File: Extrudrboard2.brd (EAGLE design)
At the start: 43.2 x 46.7 mm, 7 parts, among them U1 SN74HC138N

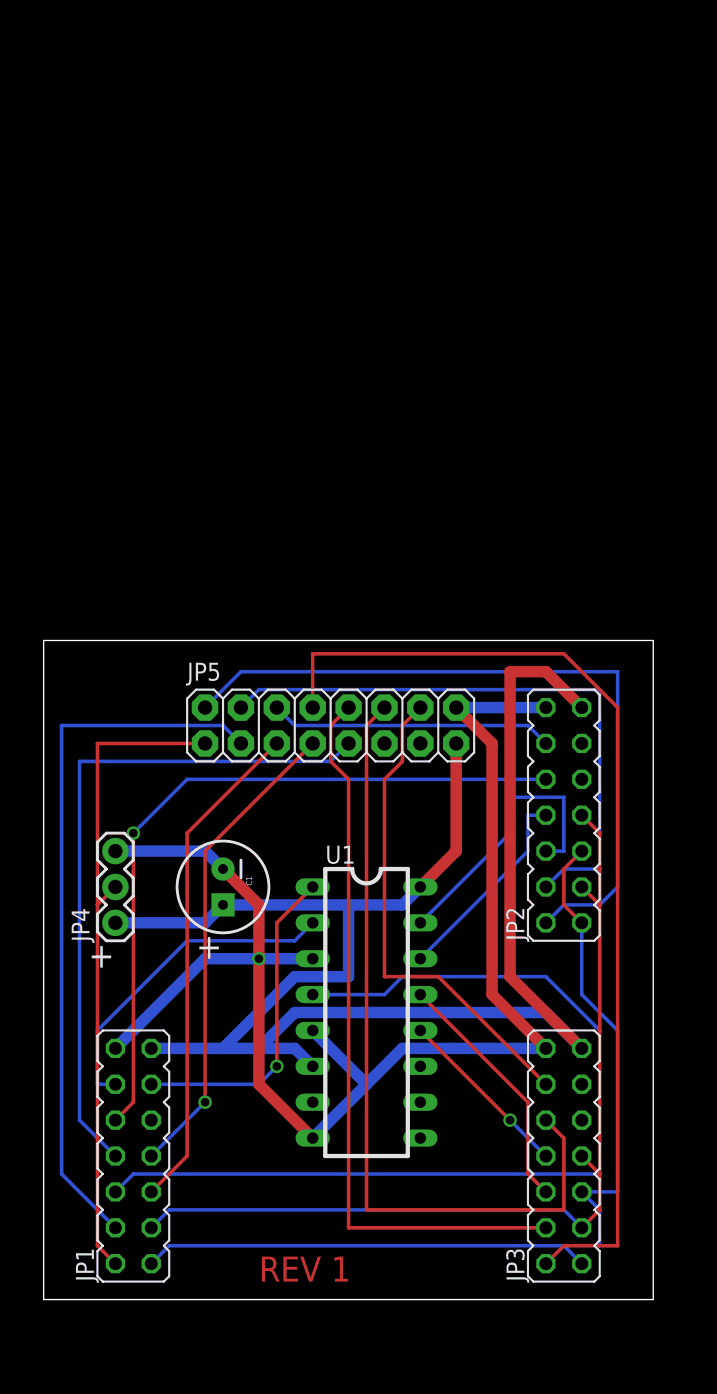
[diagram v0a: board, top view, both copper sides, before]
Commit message: Multiplex STEP instead of ENABLE.
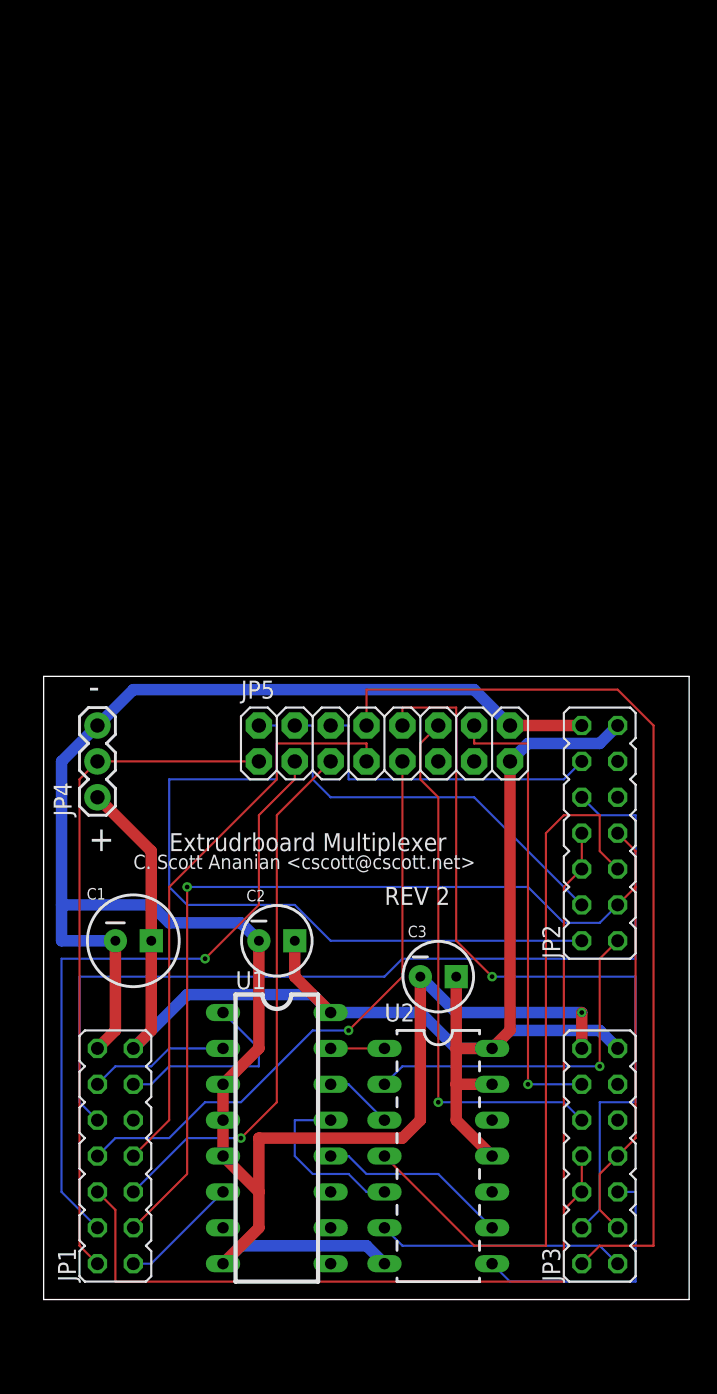
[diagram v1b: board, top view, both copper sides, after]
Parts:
- added C2, C3: 100nF, SparkFun:CPOL-RADIAL-10UF-25V
- added U2: SN74HC04, SparkFun:DIL14
- C1: value (none) -> 22uF
- moved U1 10.9 mm to (16.5, 14.0)
- moved JP4 8.98 mm to (3.81, 38.1)
- moved C1 7.41 mm to (6.35, 27.9), turned to 0 degrees
- moved JP5 4.02 mm to (15.2, 40.6)
- moved JP2 2.84 mm to (39.4, 35.6)
- moved JP3 2.54 mm to (39.4, 12.7)
- moved JP1 1.27 mm to (5.08, 12.7)
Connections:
- removed net A-ENABLE: JP2.6, U1.15
- removed net B-ENABLE: JP2.8, U1.14
- removed net C-ENABLE: JP3.6, U1.13
- removed net D-ENABLE: JP3.8, U1.12
- new net !A-STEP: U1.15, U2.1
- new net !B-STEP: U1.14, U2.3
- new net !C-STEP: U1.13, U2.5
- new net !D-STEP: U1.12, U2.9
- new net A-STEP: JP2.1, U2.2
- new net B-STEP: JP2.5, U2.4
- new net C-STEP: JP3.1, U2.6
- new net D-STEP: JP3.5, U2.8
- net E-ENABLE: now also JP2.6, JP2.8, JP3.6, JP3.8; no longer U1.4
- net E-STEP: now also U1.6; no longer JP2.1, JP2.5, JP3.1, JP3.5
- net GND: now also C2.2, C3.2, U1.4, U2.7
- net VCC: now also C2.1, C3.1, U2.11, U2.13, U2.14; no longer U1.6
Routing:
- net E-STEP: track 67.2 -> 8.45 mm
- net GND: track 104.1 -> 159.1 mm
- net B-STEP: track 0.00 -> 51.9 mm
- net A-STEP: track 0.00 -> 25.2 mm, vias 0 -> 1
- net E-DIR: track 65.4 -> 89.6 mm, vias 0 -> 1
- net A-ENABLE: track 20.4 -> 0.00 mm
- net X2_HOTENDA: track 56.9 -> 38.4 mm, vias 0 -> 1
- net D-STEP: track 0.00 -> 18.3 mm
- net C-ENABLE: track 17.7 -> 0.00 mm
- net C-STEP: track 0.00 -> 17.6 mm
- net X1_BTHERM: track 43.0 -> 27.8 mm
- net B-ENABLE: track 14.6 -> 0.00 mm
- net E_MUX1: track 23.5 -> 9.94 mm
- net !D-STEP: track 0.00 -> 13.5 mm
- net FAN2: track 51.6 -> 65.1 mm, vias 1 -> 0
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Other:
- board size 43.2 x 46.7 mm -> 45.7 x 44.1 mm
- board text added: "-"
- board text added: "CSA 2017-07-19"
- board text added: "REV 2"
- board text removed: "2017-07-18"
- board text removed: "REV 1"

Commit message: Rename Extrudrboard to Extrudrboard2 for clarity.
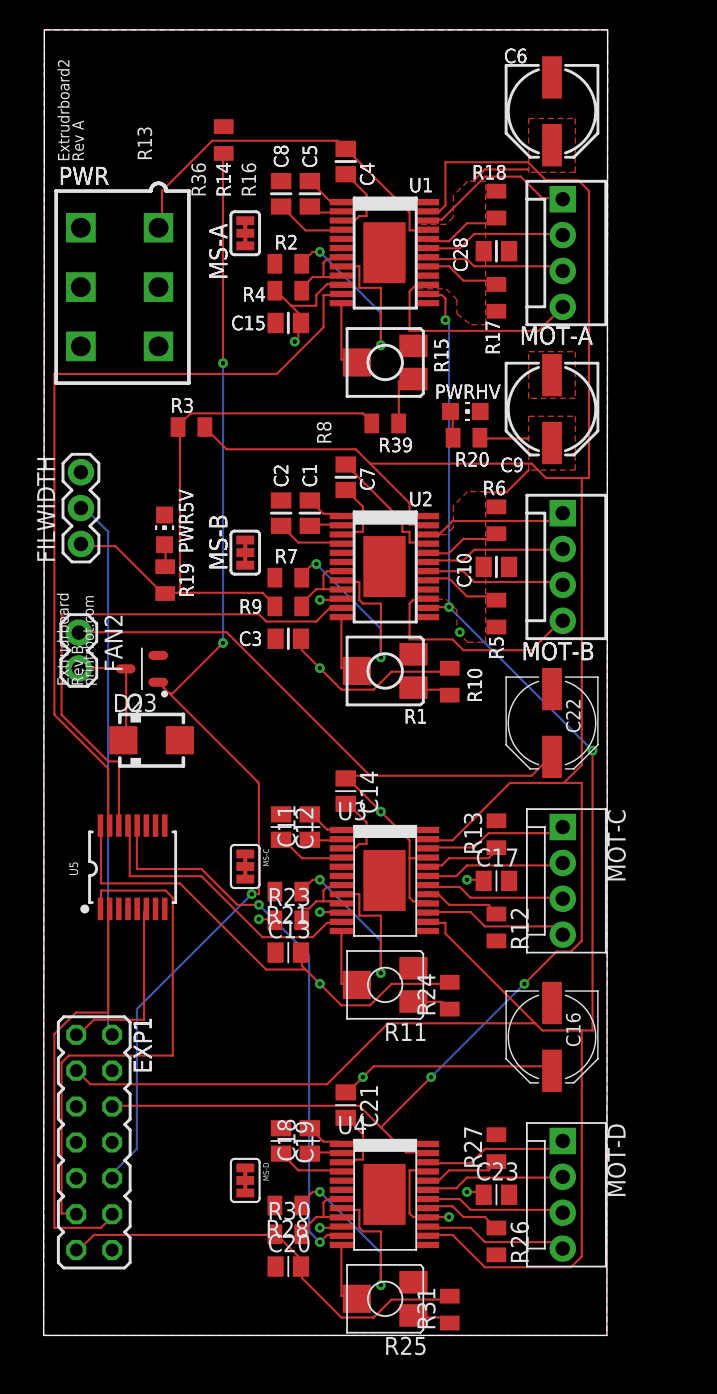
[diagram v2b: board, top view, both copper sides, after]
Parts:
- removed JP1: Printrboard, printrbot:JP7Q
- removed JP2: Extrudrboard #1, printrbot:JP7Q
- removed JP3: Extrudrboard #2, printrbot:JP7Q
- removed JP4: FILWIDTH, SparkFun:1X03
- removed JP5: Expansion, SparkFun:2X8
- added C10, C11, C14, C17, C18, C21, C23, C28, C4, C5, C7: 0.1uF, ipc-7351-capacitor:CAPC2012X145AN
- added C12, C19, C8: 0.22uF, ipc-7351-capacitor:CAPC2012X145AN
- added C13, C15, C20: 10uF, ipc-7351-capacitor:CAPC2012X145AN
- added C16, C22, C6, C9: 100uF, rcl:PANASONIC_D
- added D2: (no value), printrbot:SMA
- added EXP1: PB-E1, printrbot:JP7Q
- added FAN2: FAN, SparkFun:1X02
- added FILWIDTH: FILWIDTH, SparkFun:1X03
- added MOT-A: MOT-A, SparkFun:MOLEX-1X4
- added MOT-B: MOT-B, SparkFun:MOLEX-1X4
- added MOT-C: MOT-C, SparkFun:MOLEX-1X4
- added MOT-D: MOT-D, SparkFun:MOLEX-1X4
- added MS-A, MS-B, MS-C, MS-D: (no value), printrbot:SJ_3_CONNECTED
- added PWR: 5566-6, printrbot:5566-6
- added PWR5V, PWRHV: PWR, led:CHIP-LED0805
- added Q3: RFP30N06LE, ipc-7351-transistor:SOT95P280X135-3N
- added R1, R11, R15, R25: 10k, printrbot:RTRIM-ST4ETB
- added R10, R24, R31, R39: 20k, ipc-7351-resistor:RESC2012X70N
- added R12, R13, R17, R18, R26, R27, R5, R6: 0.11, ipc-7351-resistor:RESC2012X70N
- added R14, R23, R3, R30, R4, R9: 100k, ipc-7351-resistor:RESC2012X70N
- added R19: 330, ipc-7351-resistor:RESC2012X70N
- added R2, R21, R28, R7: 10k, ipc-7351-resistor:RESC2012X70N
- added R20: 1k, ipc-7351-resistor:RESC2012X70N
- added U3, U4: A4982, printrbot:TSSOP-24
- added U5: MC74HC238ADTR2G, mux:TSSOP16
- C1: value 22uF -> 0.1uF; device SparkFun:CPOL-RADIAL-100UF-25V -> ipc-7351-capacitor:CAPC2012X145AN
- C2: value 100nF -> 0.22uF; device SparkFun:CPOL-RADIAL-10UF-25V -> ipc-7351-capacitor:CAPC2012X145AN
- C3: value 100nF -> 10uF; device SparkFun:CPOL-RADIAL-10UF-25V -> ipc-7351-capacitor:CAPC2012X145AN
- U1: value SN74HC138N -> A4982; device SparkFun:DIL16 -> printrbot:TSSOP-24
- U2: value SN74HC04 -> A4982; device SparkFun:DIL14 -> printrbot:TSSOP-24
- moved U1 63.1 mm to (24.2, 76.6)
- moved U2 43.1 mm to (24.2, 54.4)
- moved C1 32.8 mm to (18.8, 58.2), turned to 90 degrees
- moved C2 30.3 mm to (16.8, 58.2), turned to 270 degrees
- moved C3 26.2 mm to (17.3, 49.3)
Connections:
- removed net !A-STEP: U1.15, U2.1
- removed net !B-STEP: U1.14, U2.3
- removed net !C-STEP: U1.13, U2.5
- removed net !D-STEP: U1.12, U2.9
- removed net A3: JP1.4, JP5.3
- removed net E-ENABLE: JP1.6, JP2.6, JP2.8, JP3.6, JP3.8
- removed net E_MUX0: JP1.11, U1.1
- removed net E_MUX1: JP1.12, U1.2
- removed net FAN2: JP1.10, JP2.10
- removed net PD2: JP1.5, JP5.5
- removed net PD3: JP1.7, JP5.7
- removed net TMS: JP1.8, JP5.9
- removed net VCC: C1.1, C2.1, C3.1, JP1.13, JP2.13, JP3.13, JP4.1, JP5.15, U1.16, U2.11, U2.13, U2.14
- removed net X1_ATHERM: JP2.2, JP5.2
- removed net X1_BTHERM: JP2.4, JP5.4
- removed net X1_HOTENDB: JP2.12, JP5.6
- removed net X2_ATHERM: JP3.2, JP5.8
- removed net X2_BTHERM: JP3.4, JP5.10
- removed net X2_HOTENDA: JP3.10, JP5.12
- removed net X2_HOTENDB: JP3.12, JP5.14
- new net !E-ENABLE: EXP1.6, R3.2, U1.23, U2.23, U3.23, U4.23
- new net !PWM-FAN2: EXP1.10, Q3.1, R14.1
- new net +5V: C13.2, C15.2, C20.2, C3.2, EXP1.13, FILWIDTH.1, MS-A.2, MS-B.2, MS-C.2, MS-D.2, R10.2, R19.2, R23.1, R24.2, R3.1, R30.1, R31.2, R39.2, R4.1, R9.1, U1.10, U2.10, U3.10, U4.10, U5.16
- new net 12V: C10.1, C14.1, C16.+, C17.1, C21.1, C22.+, C23.1, C28.1, C4.1, C6.+, C7.1, C9.+, FAN2.1, PWR.1, PWR.2, PWR.3, R20.2, U1.16, U1.21, U2.16, U2.21, U3.16, U3.21, U4.16, U4.21
- new net E-MUX0: EXP1.11, U5.1
- new net E-MUX1: EXP1.12, U5.2
- new net N$1: C1.2, U2.1
- new net N$10: MOT-A.3, U1.18
- new net N$11: C5.2, U1.1
- new net N$12: C5.1, U1.2
- new net N$13: R2.1, U1.8
- new net N$14: R17.1, U1.17
- new net N$15: R18.1, U1.20
- new net N$16: C4.2, U1.3
- new net N$17: MOT-A.4, U1.15
- new net N$18: R15.W, U1.12
- new net N$19: C8.2, U1.4
- new net N$2: C1.1, U2.2
- new net N$20: MOT-A.2, U1.19
- new net N$21: R4.2, U1.7, U1.9
- new net N$22: MS-B.1, U2.5
- new net N$23: MOT-A.1, U1.22
- new net N$24: MS-B.3, U2.6
- new net N$25: MOT-B.3, U2.18
- new net N$26: MOT-B.4, U2.15
- new net N$27: MS-A.1, U1.5
- new net N$28: MS-A.3, U1.6
- new net N$29: MOT-B.2, U2.19
- new net N$3: R5.1, U2.17
- new net N$30: MOT-B.1, U2.22
- new net N$31: R1.1, R10.1
- new net N$33: PWR5V.A, R19.1
- new net N$34: PWRHV.A, R20.1
- new net N$35: C11.2, U3.1
- new net N$36: C11.1, U3.2
- new net N$37: R12.1, U3.17
- new net N$38: R13.1, U3.20
- new net N$39: R11.W, U3.12
- new net N$4: R6.1, U2.20
- new net N$40: R21.1, U3.8
- new net N$41: C12.2, U3.4
- new net N$42: R23.2, U3.7, U3.9
- new net N$43: C14.2, U3.3
- new net N$44: MS-C.1, U3.5
- new net N$45: MS-C.3, U3.6
- new net N$46: MOT-C.3, U3.18
- new net N$47: MOT-C.4, U3.15
- new net N$48: MOT-C.2, U3.19
- new net N$49: MOT-C.1, U3.22
- new net N$5: R1.W, U2.12
- new net N$50: R11.1, R24.1
- new net N$51: C18.2, U4.1
- new net N$52: C18.1, U4.2
- new net N$53: R26.1, U4.17
- new net N$54: R27.1, U4.20
- new net N$55: R25.W, U4.12
- new net N$56: R28.1, U4.8
- new net N$57: C19.2, U4.4
- new net N$58: R30.2, U4.7, U4.9
- new net N$59: C21.2, U4.3
- new net N$6: R7.1, U2.8
- new net N$60: MS-D.1, U4.5
- new net N$61: MS-D.3, U4.6
- new net N$62: MOT-D.3, U4.18
- new net N$63: MOT-D.4, U4.15
- new net N$64: MOT-D.2, U4.19
- new net N$65: MOT-D.1, U4.22
- new net N$66: R25.1, R31.1
- new net N$67: D2.C, FAN2.2, Q3.3
- new net N$69: R15.1, R39.1
- new net N$7: C2.2, U2.4
- new net N$8: R9.2, U2.7, U2.9
- new net N$9: C7.2, U2.3
- net A-STEP: now also U1.11, U5.15; no longer JP2.1, U2.2
- net B-STEP: now also U2.11, U5.14; no longer JP2.5, U2.4
- net C-STEP: now also U3.11, U5.13; no longer JP3.1, U2.6
- net D-STEP: now also U4.11, U5.12; no longer JP3.5, U2.8
- net E-DIR: now also EXP1.3, U1.14, U2.14, U3.14, U4.14; no longer JP1.3, JP2.3, JP2.7, JP3.3, JP3.7
- net E-STEP: now also EXP1.1, U5.6; no longer JP1.1, U1.6
- net FILWIDTH: now also EXP1.2, FILWIDTH.2; no longer JP1.2, JP4.2, JP5.1
- net GND: now also C10.2, C12.1, C13.1, C15.1, C16.-, C17.2, C19.1, C2.1, C20.1, C22.-, C23.2, C28.2, C3.1, C6.-, C8.1, C9.-, D2.A, EXP1.14, FILWIDTH.3, PWR.4, PWR.5, PWR.6, PWR5V.C, PWRHV.C, Q3.2, R1.2, R11.2, R12.2, R13.2, R14.2, R15.2, R17.2, R18.2, R2.2, R21.2, R25.2, R26.2, R27.2, R28.2, R5.2, R6.2, R7.2, U1.13, U1.24, U1.PAD, U2.13, U2.24, U2.PAD, U3.13, U3.24, U3.PAD, U4.13, U4.24, U4.PAD, U5.3, U5.4, U5.5, U5.8; no longer C1.2, C2.2, C3.2, JP1.14, JP2.14, JP3.14, JP4.3, JP5.16, U1.3, U1.4, U1.5, U1.8, U2.7
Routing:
- net !E-ENABLE: track 0.00 -> 160.7 mm, vias 0 -> 2
- net GND: track 159.1 -> 0.06 mm, vias 1 -> 0
- net +5V: track 0.00 -> 135.5 mm, vias 0 -> 7
- net 12V: track 0.00 -> 125.5 mm, vias 0 -> 6
- net VCC: track 112.9 -> 0.00 mm
- net !PWM-FAN2: track 0.00 -> 82.7 mm, vias 0 -> 3
- net E-ENABLE: track 75.2 -> 0.00 mm
- net X2_ATHERM: track 66.3 -> 0.00 mm
- net FAN2: track 65.1 -> 0.00 mm
- net X2_BTHERM: track 56.2 -> 0.00 mm, vias 1 -> 0
- net X1_ATHERM: track 51.1 -> 0.00 mm
- net E-DIR: track 89.6 -> 137.2 mm, vias 1 -> 3
- net A3: track 46.9 -> 0.00 mm, vias 1 -> 0
- net TMS: track 42.1 -> 0.00 mm, vias 1 -> 0
- net PD3: track 41.0 -> 0.00 mm
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- added copper zone on layer 3, net +5V
- added copper zone on layer 1, net 12V
- added copper zone on layer 3, net 12V
- added copper zone on layer 1, net GND
- added copper zone on layer 16, net GND
- added copper zone on layer 2, net GND
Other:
- board size 45.7 x 44.1 mm -> 39.9 x 92.4 mm
- board text added: "C1"
- board text added: "C10"
- board text added: "C15"
- board text added: "C2"
- board text added: "C28"
- board text added: "C3"
- board text added: "C4"
- board text added: "C5"
- board text added: "C6"
- board text added: "C7"
- board text added: "C8"
- board text added: "C9"
- board text added: "EXP1"
- board text added: "Extrudrboard"
- board text added: "Extrudrboard2"
- board text added: "Laine Walker-Avina (C) 2013"
- board text added: "MOT-A"
- board text added: "MOT-B"
- board text added: "MS-A"
- board text added: "MS-B"
- board text added: "PWR"
- board text added: "PWR5V"
- board text added: "PWRHV"
- board text added: "R1"
- board text added: "R10"
- board text added: "R13"
- board text added: "R14"
- board text added: "R15"
- board text added: "R16"
- board text added: "R17"
- board text added: "R18"
- board text added: "R19"
- board text added: "R2"
- board text added: "R20"
- board text added: "R3"
- board text added: "R36"
- board text added: "R39"
- board text added: "R4"
- board text added: "R5"
- board text added: "R6"
- board text added: "R7"
- board text added: "R8"
- board text added: "R9"
- board text added: "Rev A"
- board text added: "Rev B"
- board text added: "U1"
- board text added: "U2"
- board text added: "printrbot.com"
- board text removed: "+"
- board text removed: "-"
- board text removed: "1"
- board text removed: "C. Scott Ananian <cscott@cscott.net>"
- board text removed: "CSA 2017-07-19"
- board text removed: "Extrudrboard Multiplexer"
- board text removed: "REV 2"
